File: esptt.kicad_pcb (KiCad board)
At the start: 2 copper layers, 2 parts

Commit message: antenna
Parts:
- added >NAME: >VALUE, OPL-Antenna:OPL-Antenna-ANT2-SMD-9.5X2.1X1.0MM, F.Cu at (139.2, 91.7)
- moved ESP-06 2.51 mm to (142.7, 82.2)
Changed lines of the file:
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@@
     (links 0)
     (no_connects 0)
-    (area 129.552381 35.05 155.04762 94.000001)
+    (area 129.552381 34.45 155.04762 94.000001)
     (thickness 1.6)
     (drawings 7)
     (tracks 0)
     (zones 0)
-    (modules 2)
+    (modules 3)
     (nets 1)
   )
@@
     (uvia_drill 0.1)
   )
+  (module OPL-Antenna:OPL-Antenna-ANT2-SMD-9.5X2.1X1.0MM (layer F.Cu)
+    (at 139.2 91.7)
+    (attr smd)
+    (fp_text reference >NAME (at 0.3175 -1.7145) (layer B.SilkS)
+      (effects (font (size 0.889 0.889) (thickness 0.0889)))
+    )
+    (fp_text value >VALUE (at 0.762 2.0955) (layer B.SilkS)
+      (effects (font (size 0.889 0.889) (thickness 0.0889)))
+    )
+    (fp_line (start -4.7498 1.04902) (end 4.7498 1.04902) (layer F.SilkS) (width 0.06604))
+    (fp_line (start 4.7498 1.04902) (end 4.7498 -1.04902) (layer F.SilkS) (width 0.06604))
+    (fp_line (start -4.7498 -1.04902) (end 4.7498 -1.04902) (layer F.SilkS) (width 0.06604))
+    (fp_line (start -4.7498 1.04902) (end -4.7498 -1.04902) (layer F.SilkS) (width 0.06604))
+    (fp_line (start -4.7498 -1.04902) (end 4.7498 -1.04902) (layer F.SilkS) (width 0.127))
+    (fp_line (start 4.7498 -1.04902) (end 4.7498 1.04902) (layer F.SilkS) (width 0.127))
+    (fp_line (start 4.7498 1.04902) (end -4.7498 1.04902) (layer F.SilkS) (width 0.127))
+    (fp_line (start -4.7498 1.04902) (end -4.7498 -1.04902) (layer F.SilkS) (width 0.127))
+    (fp_circle (center -6.35 0) (end -6.5405 0.1905) (layer F.SilkS) (width 0))
+    (pad 1 smd rect (at -4.7498 0) (size 1.39954 2.09804) (layers F.Cu F.Paste F.Mask))
+    (pad 2 smd rect (at 4.7498 0) (size 1.39954 2.09804) (layers F.Cu F.Paste F.Mask))
+  )
   (module ESP-06 (layer F.Cu)
-    (at 142.5 84.7)
+    (at 142.7 82.2)
     (fp_text reference ESP-06 (at 0 0.5) (layer F.SilkS)
       (effects (font (size 1 1) (thickness 0.15)))

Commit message: regulator
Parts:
- added >NAME: >VALUE, aalay:aalay-SOT223, F.Cu at (142.2, 52.4)
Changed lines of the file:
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@@
     (tracks 0)
     (zones 0)
-    (modules 3)
+    (modules 4)
     (nets 1)
   )
@@
     (uvia_drill 0.1)
   )
+  (module aalay:aalay-SOT223 (layer F.Cu)
+    (at 142.2 52.4)
+    (descr "SOT223 PACKAGE")
+    (tags "SOT223 PACKAGE")
+    (attr smd)
+    (fp_text reference >NAME (at 0.635 -0.6858) (layer B.SilkS)
+      (effects (font (size 1.27 1.27) (thickness 0.0889)))
+    )
+    (fp_text value >VALUE (at 1.27 0.6858) (layer B.SilkS)
+      (effects (font (size 1.27 1.27) (thickness 0.0889)))
+    )
+    (fp_line (start -1.6002 -1.80086) (end 1.6002 -1.80086) (layer F.SilkS) (width 0.06604))
+    (fp_line (start 1.6002 -1.80086) (end 1.6002 -3.6576) (layer F.SilkS) (width 0.06604))
+    (fp_line (start -1.6002 -3.6576) (end 1.6002 -3.6576) (layer F.SilkS) (width 0.06604))
+    (fp_line (start -1.6002 -1.80086) (end -1.6002 -3.6576) (layer F.SilkS) (width 0.06604))
+    (fp_line (start -0.4318 3.6576) (end 0.4318 3.6576) (layer F.SilkS) (width 0.06604))
+    (fp_line (start 0.4318 3.6576) (end 0.4318 1.80086) (layer F.SilkS) (width 0.06604))
+    (fp_line (start -0.4318 1.80086) (end 0.4318 1.80086) (layer F.SilkS) (width 0.06604))
+    (fp_line (start -0.4318 3.6576) (end -0.4318 1.80086) (layer F.SilkS) (width 0.06604))
+    (fp_line (start -2.7432 3.6576) (end -1.8796 3.6576) (layer F.SilkS) (width 0.06604))
+    (fp_line (start -1.8796 3.6576) (end -1.8796 1.80086) (layer F.SilkS) (width 0.06604))
+    (fp_line (start -2.7432 1.80086) (end -1.8796 1.80086) (layer F.SilkS) (width 0.06604))
+    (fp_line (start -2.7432 3.6576) (end -2.7432 1.80086) (layer F.SilkS) (width 0.06604))
+    (fp_line (start 1.8796 3.6576) (end 2.7432 3.6576) (layer F.SilkS) (width 0.06604))
+    (fp_line (start 2.7432 3.6576) (end 2.7432 1.80086) (layer F.SilkS) (width 0.06604))
+    (fp_line (start 1.8796 1.80086) (end 2.7432 1.80086) (layer F.SilkS) (width 0.06604))
+    (fp_line (start 1.8796 3.6576) (end 1.8796 1.80086) (layer F.SilkS) (width 0.06604))
+    (fp_line (start -1.6002 -1.80086) (end 1.6002 -1.80086) (layer F.SilkS) (width 0.06604))
+    (fp_line (start 1.6002 -1.80086) (end 1.6002 -3.6576) (layer F.SilkS) (width 0.06604))
+    (fp_line (start -1.6002 -3.6576) (end 1.6002 -3.6576) (layer F.SilkS) (width 0.06604))
+    (fp_line (start -1.6002 -1.80086) (end -1.6002 -3.6576) (layer F.SilkS) (width 0.06604))
+    (fp_line (start -0.4318 3.6576) (end 0.4318 3.6576) (layer F.SilkS) (width 0.06604))
+    (fp_line (start 0.4318 3.6576) (end 0.4318 1.80086) (layer F.SilkS) (width 0.06604))
+    (fp_line (start -0.4318 1.80086) (end 0.4318 1.80086) (layer F.SilkS) (width 0.06604))
+    (fp_line (start -0.4318 3.6576) (end -0.4318 1.80086) (layer F.SilkS) (width 0.06604))
+    (fp_line (start -2.7432 3.6576) (end -1.8796 3.6576) (layer F.SilkS) (width 0.06604))
+    (fp_line (start -1.8796 3.6576) (end -1.8796 1.80086) (layer F.SilkS) (width 0.06604))
+    (fp_line (start -2.7432 1.80086) (end -1.8796 1.80086) (layer F.SilkS) (width 0.06604))
+    (fp_line (start -2.7432 3.6576) (end -2.7432 1.80086) (layer F.SilkS) (width 0.06604))
+    (fp_line (start 1.8796 3.6576) (end 2.7432 3.6576) (layer F.SilkS) (width 0.06604))
+    (fp_line (start 2.7432 3.6576) (end 2.7432 1.80086) (layer F.SilkS) (width 0.06604))
+    (fp_line (start 1.8796 1.80086) (end 2.7432 1.80086) (layer F.SilkS) (width 0.06604))
+    (fp_line (start 1.8796 3.6576) (end 1.8796 1.80086) (layer F.SilkS) (width 0.06604))
+    (fp_line (start 3.2766 -1.778) (end 3.2766 1.778) (layer F.SilkS) (width 0.2032))
+    (fp_line (start 3.2766 1.778) (end -3.2766 1.778) (layer F.SilkS) (width 0.2032))
+    (fp_line (start -3.2766 1.778) (end -3.2766 -1.778) (layer F.SilkS) (width 0.2032))
+    (fp_line (start -3.2766 -1.778) (end 3.2766 -1.778) (layer F.SilkS) (width 0.2032))
+    (pad 1 smd rect (at -2.30886 3.0988) (size 1.21666 2.23266) (layers F.Cu F.Paste F.Mask))
+    (pad 2 smd rect (at 0 3.0988) (size 1.21666 2.23266) (layers F.Cu F.Paste F.Mask))
+    (pad 3 smd rect (at 2.30886 3.0988) (size 1.21666 2.23266) (layers F.Cu F.Paste F.Mask))
+    (pad 4 smd rect (at 0 -3.0988) (size 3.59918 2.19964) (layers F.Cu F.Paste F.Mask))
+  )
   (module OPL-Antenna:OPL-Antenna-ANT2-SMD-9.5X2.1X1.0MM (layer F.Cu)

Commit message: first wire
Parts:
- turned LM1117 to 180 degrees
- renumbered >NAME to LM1117
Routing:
- net (no net): track 0.00 -> 6.58 mm
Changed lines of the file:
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@@
     (thickness 1.6)
     (drawings 7)
-    (tracks 0)
+    (tracks 3)
     (zones 0)
     (modules 4)
@@
   )
   (module aalay:aalay-SOT223 (layer F.Cu)
-    (at 142.2 52.4)
+    (at 142.2 52.4 180)
     (descr "SOT223 PACKAGE")
     (tags "SOT223 PACKAGE")
     (attr smd)
-    (fp_text reference >NAME (at 0.635 -0.6858) (layer B.SilkS)
-      (effects (font (size 1.27 1.27) (thickness 0.0889)))
-    )
-    (fp_text value >VALUE (at 1.27 0.6858) (layer B.SilkS)
-      (effects (font (size 1.27 1.27) (thickness 0.0889)))
+    (fp_text reference LM1117 (at 0 -0.5 180) (layer F.SilkS)
+      (effects (font (size 1.27 1) (thickness 0.0889)))
+    )
+    (fp_text value >VALUE (at 1.27 0.6858 180) (layer B.SilkS) hide
+      (effects (font (size 1.27 1.27) (thickness 0.0889)) (justify mirror))
     )
     (fp_line (start -1.6002 -1.80086) (end 1.6002 -1.80086) (layer F.SilkS) (width 0.06604))
@@
     (fp_line (start -3.2766 1.778) (end -3.2766 -1.778) (layer F.SilkS) (width 0.2032))
     (fp_line (start -3.2766 -1.778) (end 3.2766 -1.778) (layer F.SilkS) (width 0.2032))
-    (pad 1 smd rect (at -2.30886 3.0988) (size 1.21666 2.23266) (layers F.Cu F.Paste F.Mask))
-    (pad 2 smd rect (at 0 3.0988) (size 1.21666 2.23266) (layers F.Cu F.Paste F.Mask))
-    (pad 3 smd rect (at 2.30886 3.0988) (size 1.21666 2.23266) (layers F.Cu F.Paste F.Mask))
-    (pad 4 smd rect (at 0 -3.0988) (size 3.59918 2.19964) (layers F.Cu F.Paste F.Mask))
+    (pad 1 smd rect (at -2.30886 3.0988 180) (size 1.21666 2.23266) (layers F.Cu F.Paste F.Mask))
+    (pad 2 smd rect (at 0 3.0988 180) (size 1.21666 2.23266) (layers F.Cu F.Paste F.Mask))
+    (pad 3 smd rect (at 2.30886 3.0988 180) (size 1.21666 2.23266) (layers F.Cu F.Paste F.Mask))
+    (pad 4 smd rect (at 0 -3.0988 180) (size 3.59918 2.19964) (layers F.Cu F.Paste F.Mask))
   )
   (module OPL-Antenna:OPL-Antenna-ANT2-SMD-9.5X2.1X1.0MM (layer F.Cu)
@@
     (tags "USB USB_B USB_micro USB_OTG")
     (attr smd)
-    (fp_text reference REF** (at -1.5 -4.625 180) (layer F.SilkS)
+    (fp_text reference REF** (at -1.5 -4.625 180) (layer F.SilkS) hide
       (effects (font (size 1 1) (thickness 0.15)))
     )
@@
   (gr_line (start 153.3 93.9) (end 153.3 70.4) (angle 90) (layer F.SilkS) (width 0.2))
   (gr_line (start 131.9 93.9) (end 153.3 93.9) (angle 90) (layer F.SilkS) (width 0.2))
+  (segment (start 144.50886 49.3012) (end 144.50886 46.20886) (width 0.25) (layer F.Cu) (net 0))
+  (segment (start 143.6 45.3) (end 143.6 43.1) (width 0.25) (layer F.Cu) (net 0))
+  (segment (start 144.50886 46.20886) (end 143.6 45.3) (width 0.25) (layer F.Cu) (net 0))
 )

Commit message: lot of bits
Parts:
- added LIGHT: Pin_Header_Straight_1x03, Pin_Headers:Pin_Header_Straight_1x03, F.Cu at (150.0, 51.4)
- added Pgr: Pin_Header_Straight_1x05, Pin_Headers:Pin_Header_Straight_1x05, F.Cu at (135.0, 44.2)
- added RGB: Pin_Header_Straight_1x03, Pin_Headers:Pin_Header_Straight_1x03, F.Cu at (138.9, 79.1)
- added TEMP: Pin_Header_Straight_1x03, Pin_Headers:Pin_Header_Straight_1x03, F.Cu at (149.9, 41.0)
- added pwr: >VALUE, aalay:aalay-LED1206, F.Cu at (134.9, 39.9)
- added status: >VALUE, aalay:aalay-LED1206, F.Cu at (150.5, 61.5)
- moved ANT 23.0 mm to (151.0, 72.0), turned to 90 degrees
- moved ESP-06 14.5 mm to (141.2, 67.8), turned to 90 degrees
- moved LM1117 0.81 mm to (142.3, 51.6), turned to 0 degrees
- renumbered >NAME to ANT
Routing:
- net (no net): track 6.58 -> 394.6 mm, vias 0 -> 9
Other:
- board outline added: 21.3 x 43 mm
- board text added: "+3"
- board text added: "+5"
- board text added: "D"
- board text added: "G"
- board text added: "G0"
- board text added: "RX"
- board text added: "TX"
- board text added: "WIFI"
- board text added: "donp.org ESP RGB 2016 March"

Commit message: July 2016
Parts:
- removed Pgr: Pin_Header_Straight_1x05, Pin_Headers:Pin_Header_Straight_1x05
- added ?: Pin_Header_Straight_1x06, Pin_Headers:Pin_Header_Straight_1x06, F.Cu at (135.1, 44.2)
- added ?: R_0603, Resistors_SMD:R_0603, F.Cu at (146.8, 58.2)
- added ?: R_0603, Resistors_SMD:R_0603, F.Cu at (136.7, 41.4)
- added ?: MountingHole_2.2mm_M2, Mounting_Holes:MountingHole_2.2mm_M2, F.Cu at (133.9, 79.5)
- added ?: MountingHole_2.2mm_M2, Mounting_Holes:MountingHole_2.2mm_M2, F.Cu at (151.4, 79.5)
- added C1: C_0603, Capacitors_SMD:C_0603, F.Cu at (142.5, 56.5)
- added R1: R_0603, Resistors_SMD:R_0603, F.Cu at (137.7, 53.8)
- added R2: R_0603, Resistors_SMD:R_0603, F.Cu at (137.7, 57.4)
- added REF**: R_0603, Resistors_SMD:R_0603, F.Cu at (149.1, 64.0)
- WIFI ANT: renamed from ANT
- moved LM1117 1.12 mm to (142.5, 50.5)
- moved NeoPx 0.81 mm to (139.7, 79.0)
- moved status 0.67 mm to (151.1, 61.7)
- moved pwr 0.53 mm to (134.9, 39.4)
- moved ESP-06 0.48 mm to (140.7, 67.8)
- renumbered RGB to NeoPx
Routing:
- net (no net): track 394.6 -> 422.8 mm, vias 9 -> 13
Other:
- board text added: "G2"
- board text added: "donp.org ESP-FTL 2016 July"
- board text removed: "WIFI"
- board text removed: "donp.org ESP RGB 2016 March"

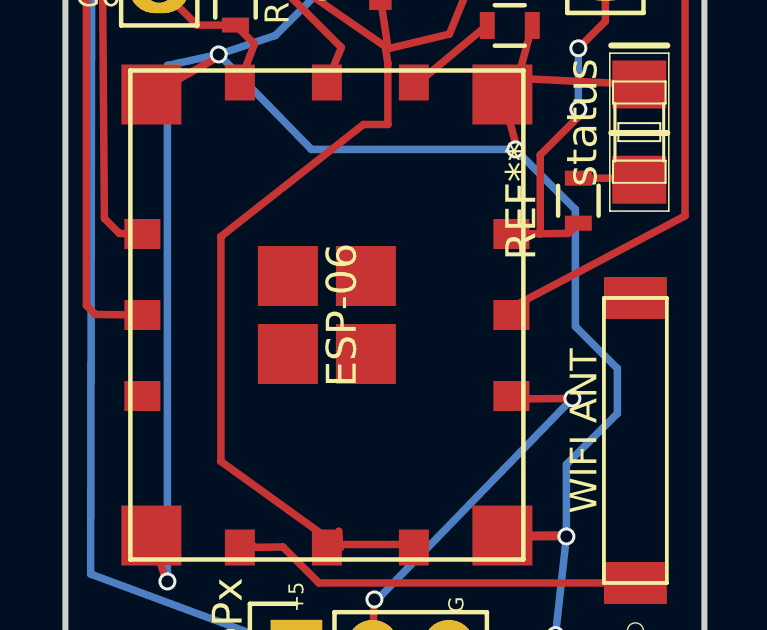
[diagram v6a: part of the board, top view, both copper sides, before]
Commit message: Start 2016-Aug. tie the center grounds.
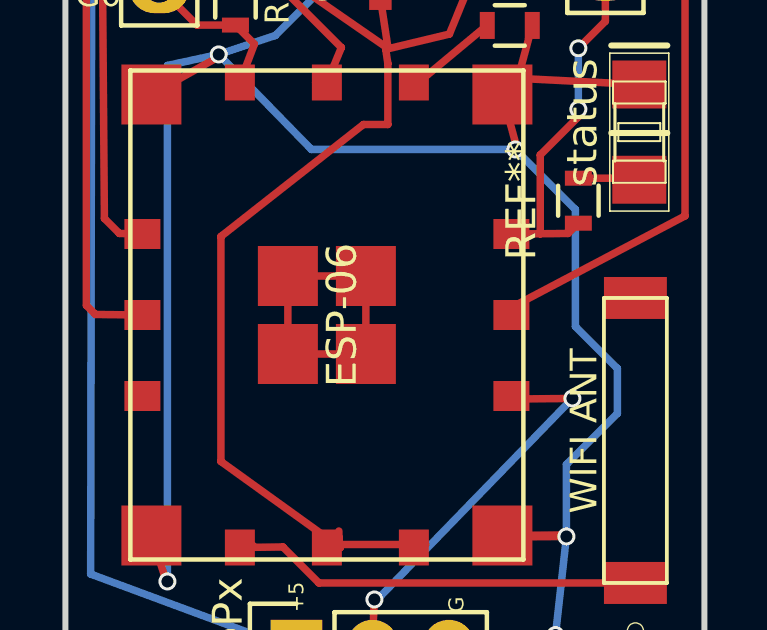
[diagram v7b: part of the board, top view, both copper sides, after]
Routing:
- net (no net): track 422.8 -> 433.2 mm
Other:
- board text added: "donp.org ESP-FTL 2016 Aug"
- board text removed: "donp.org ESP-FTL 2016 July"
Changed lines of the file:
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@@
     (thickness 1.6)
     (drawings 19)
-    (tracks 159)
+    (tracks 163)
     (zones 0)
     (modules 18)
@@
     (34 B.Paste user hide)
     (35 F.Paste user)
-    (36 B.SilkS user)
-    (37 F.SilkS user)
+    (36 B.SilkS user hide)
+    (37 F.SilkS user hide)
     (38 B.Mask user)
     (39 F.Mask user)
@@
   (gr_line (start 153.3 38) (end 132 38) (angle 90) (layer Edge.Cuts) (width 0.2))
   (gr_line (start 153.3 38) (end 153.3 81) (angle 90) (layer Edge.Cuts) (width 0.2))
-  (gr_text "donp.org\nESP-FTL\n2016 July" (at 142.6 73.6) (layer B.SilkS)
+  (gr_text "donp.org\nESP-FTL\n2016 Aug" (at 142.6 73.6) (layer B.SilkS)
     (effects (font (size 1.5 1.5) (thickness 0.3)) (justify mirror))
   )
+  (segment (start 139.416 66.518) (end 139.416 69.118) (width 0.25) (layer F.Cu) (net 0) (status C00000))
+  (segment (start 139.416 69.118) (end 142.016 69.118) (width 0.25) (layer F.Cu) (net 0) (status C00000))
+  (segment (start 142.016 69.118) (end 142.016 66.518) (width 0.25) (layer F.Cu) (net 0) (status C00000))
+  (segment (start 142.016 66.518) (end 139.416 66.518) (width 0.25) (layer F.Cu) (net 0) (status C00000))
   (segment (start 149.098 60.96) (end 149.098 61.214) (width 0.25) (layer F.Cu) (net 0))
   (via (at 149.098 60.96) (size 0.6) (drill 0.4) (layers F.Cu B.Cu) (net 0))

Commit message: tidy things. remove cap
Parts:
- removed C1: C_0603, Capacitors_SMD:C_0603
- moved ? 0.25 mm to (146.8, 57.9)
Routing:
- net (no net): track 433.2 -> 444.0 mm
